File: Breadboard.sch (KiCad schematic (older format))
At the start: 15 parts, among them J201 AudioJack2_SwitchT, J202 AudioJack2_SwitchT, J203 Conn_01x03_Male, J204 Conn_01x03_Male, J205 Power +, J206 Power -, P201 HEADER_2x5_Doepfer

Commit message: Update misc diags
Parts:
- added D?: On LED, AJ:D_0805_AJ, symbol Device:LED
- added J? (x2): Conn_01x03_Male, Connector_PinHeader_2.54mm:PinHeader_1x03_P2.54mm_Vertical, symbol Connector:Conn_01x03_Male
- added J?: AudioJack2_SwitchT, Connector_Audio:Jack_3.5mm_Switronic_ST-005-G_horizontal, symbol Connector:AudioJack2_SwitchT
- added R?: 22k, AJ:R_0805_AJ, symbol Device:R
- added R? (x2): OPEN, AJ:R_0805_AJ, symbol Device:R
- added RV?: 100k, AJ:Potentiometer_China_RK09_Single_Vertical_AJ, symbol Device:R_POT
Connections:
- net GND: now also J?.1 (Pin_1), J?.S
- net at D201.2 (A), R201.2: now also D?.1 (K)
- net at P201.10 (+12), P201.9 (+12), R202.2: now also R?.1
- new net: J?.2 (Pin_2), J?.T
- new net: J?.3 (Pin_3), J?.TN
- new net: D?.2 (A), R?.2
- new net: J?.1 (Pin_1), R?.2, RV?.1
- new net: J?.2 (Pin_2), R?.1, R?.2, RV?.2
- new net: J?.3 (Pin_3), R?.1, RV?.3
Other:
- moved on the sheet: J205, J206
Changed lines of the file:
@@
 L Connector:Conn_01x04_Male J205
 U 1 1 60800BD9
-P 4900 4300
-F 0 "J205" H 4872 4274 50  0000 R CNN
-F 1 "Power +" H 4872 4183 50  0000 R CNN
-F 2 "Connector_PinHeader_2.54mm:PinHeader_2x02_P2.54mm_Vertical" H 4900 4300 50  0001 C CNN
-F 3 "~" H 4900 4300 50  0001 C CNN
-	1    4900 4300
+P 5900 2100
+F 0 "J205" H 5872 2074 50  0000 R CNN
+F 1 "Power +" H 5872 1983 50  0000 R CNN
+F 2 "Connector_PinHeader_2.54mm:PinHeader_2x02_P2.54mm_Vertical" H 5900 2100 50  0001 C CNN
+F 3 "~" H 5900 2100 50  0001 C CNN
+	1    5900 2100
 	-1   0    0    -1
 $EndComp
@@
 L Connector:Conn_01x04_Male J206
 U 1 1 608011E9
-P 4900 4775
-F 0 "J206" H 4872 4749 50  0000 R CNN
-F 1 "Power -" H 4872 4658 50  0000 R CNN
-F 2 "Connector_PinHeader_2.54mm:PinHeader_2x02_P2.54mm_Vertical" H 4900 4775 50  0001 C CNN
-F 3 "~" H 4900 4775 50  0001 C CNN
-	1    4900 4775
-	-1   0    0    -1
-$EndComp
-Wire Wire Line
-	4700 4200 4525 4200
-Wire Wire Line
-	4525 4200 4525 4400
-Wire Wire Line
-	4525 4400 4700 4400
-Wire Wire Line
-	4700 4300 4600 4300
-Wire Wire Line
-	4600 4300 4600 4500
-Wire Wire Line
-	4600 4500 4700 4500
-Wire Wire Line
-	4700 4675 4525 4675
-Wire Wire Line
-	4525 4675 4525 4875
-Wire Wire Line
-	4525 4875 4700 4875
-Wire Wire Line
-	4700 4775 4600 4775
-Wire Wire Line
-	4600 4775 4600 4975
-Wire Wire Line
-	4600 4975 4700 4975
-Text GLabel 4600 4975 0    50   Input ~ 0
+P 5900 2575
+F 0 "J206" H 5872 2549 50  0000 R CNN
+F 1 "Power -" H 5872 2458 50  0000 R CNN
+F 2 "Connector_PinHeader_2.54mm:PinHeader_2x02_P2.54mm_Vertical" H 5900 2575 50  0001 C CNN
+F 3 "~" H 5900 2575 50  0001 C CNN
+	1    5900 2575
+	-1   0    0    -1
+$EndComp
+Wire Wire Line
+	5700 2000 5525 2000
+Wire Wire Line
+	5525 2000 5525 2200
+Wire Wire Line
+	5525 2200 5700 2200
+Wire Wire Line
+	5700 2100 5600 2100
+Wire Wire Line
+	5600 2100 5600 2300
+Wire Wire Line
+	5600 2300 5700 2300
+Wire Wire Line
+	5700 2475 5525 2475
+Wire Wire Line
+	5525 2475 5525 2675
+Wire Wire Line
+	5525 2675 5700 2675
+Wire Wire Line
+	5700 2575 5600 2575
+Wire Wire Line
+	5600 2575 5600 2775
+Wire Wire Line
+	5600 2775 5700 2775
+Text GLabel 5600 2775 0    50   Input ~ 0
 -12Vc
-Text GLabel 4525 4200 0    50   Input ~ 0
+Text GLabel 5525 2000 0    50   Input ~ 0
 +12Vc
 $Comp
 L power:GND #PWR?
 U 1 1 60806A30
-P 4600 4500
+P 5600 2300
 AR Path="/60806A30" Ref="#PWR?"  Part="1"
 AR Path="/607E07E1/60806A30" Ref="#PWR0204"  Part="1"
-F 0 "#PWR0204" H 4600 4250 50  0001 C CNN
-F 1 "GND" H 4605 4327 50  0000 C CNN
-F 2 "" H 4600 4500 50  0001 C CNN
-F 3 "" H 4600 4500 50  0001 C CNN
-	1    4600 4500
+F 0 "#PWR0204" H 5600 2050 50  0001 C CNN
+F 1 "GND" H 5605 2127 50  0000 C CNN
+F 2 "" H 5600 2300 50  0001 C CNN
+F 3 "" H 5600 2300 50  0001 C CNN
+	1    5600 2300
 	1    0    0    -1
 $EndComp
-Connection ~ 4600 4500
-Wire Wire Line
-	4525 4675 4525 4500
-Connection ~ 4525 4675
-Wire Wire Line
-	4525 4500 4600 4500
+Connection ~ 5600 2300
+Wire Wire Line
+	5525 2475 5525 2300
+Connection ~ 5525 2475
+Wire Wire Line
+	5525 2300 5600 2300
 Wire Wire Line
 	3600 2350 4275 2350
@@
 Wire Wire Line
 	3600 2750 4275 2750
+$Comp
+L Connector:Conn_01x03_Male J?
+U 1 1 6086D012
+P 3175 3725
+F 0 "J?" H 3147 3749 50  0000 R CNN
+F 1 "Conn_01x03_Male" H 3147 3658 50  0000 R CNN
+F 2 "Connector_PinHeader_2.54mm:PinHeader_1x03_P2.54mm_Vertical" H 3175 3725 50  0001 C CNN
+F 3 "~" H 3175 3725 50  0001 C CNN
+	1    3175 3725
+	-1   0    0    -1
+$EndComp
+$Comp
+L Connector:AudioJack2_SwitchT J?
+U 1 1 6086D1D0
+P 2425 3725
+F 0 "J?" H 2457 4050 50  0000 C CNN
+F 1 "AudioJack2_SwitchT" H 2457 3959 50  0000 C CNN
+F 2 "Connector_Audio:Jack_3.5mm_Switronic_ST-005-G_horizontal" H 2425 3725 50  0001 C CNN
+F 3 "~" H 2425 3725 50  0001 C CNN
+	1    2425 3725
+	1    0    0    -1
+$EndComp
+Wire Wire Line
+	2625 3625 2825 3625
+Wire Wire Line
+	2625 3725 2975 3725
+Wire Wire Line
+	2625 3825 2975 3825
+Wire Wire Line
+	2825 4225 2825 3625
+Connection ~ 2825 3625
+Wire Wire Line
+	2825 3625 2975 3625
+Wire Wire Line
+	2000 2300 2000 2350
+Wire Wire Line
+	2025 1950 2000 1950
+Wire Wire Line
+	2000 1950 2000 2000
+$Comp
+L Device:R R?
+U 1 1 6086F9BC
+P 2175 1950
+AR Path="/6086F9BC" Ref="R?"  Part="1"
+AR Path="/5C8C5FC0/6086F9BC" Ref="R?"  Part="1"
+AR Path="/5D60ED9A/6086F9BC" Ref="R?"  Part="1"
+AR Path="/60565919/6086F9BC" Ref="R?"  Part="1"
+AR Path="/607E07E1/6086F9BC" Ref="R?"  Part="1"
+F 0 "R?" V 2175 1950 50  0000 C CNN
+F 1 "22k" V 2275 1950 50  0000 C CNN
+F 2 "AJ:R_0805_AJ" V 2105 1950 50  0001 C CNN
+F 3 "~" H 2175 1950 50  0001 C CNN
+	1    2175 1950
+	0    1    1    0
+$EndComp
+$Comp
+L Device:LED D?
+U 1 1 6086F9C6
+P 2000 2150
+AR Path="/5C8BFBBC/6086F9C6" Ref="D?"  Part="1"
+AR Path="/5C8C5FC0/6086F9C6" Ref="D?"  Part="1"
+AR Path="/5D60ED9A/6086F9C6" Ref="D?"  Part="1"
+AR Path="/60565919/6086F9C6" Ref="D?"  Part="1"
+AR Path="/6086F9C6" Ref="D?"  Part="1"
+AR Path="/607E07E1/6086F9C6" Ref="D?"  Part="1"
+F 0 "D?" V 2075 2375 50  0000 R CNN
+F 1 "On LED" V 2000 2425 50  0000 R CNN
+F 2 "AJ:D_0805_AJ" H 2000 2150 50  0001 C CNN
+F 3 "~" H 2000 2150 50  0001 C CNN
+	1    2000 2150
+	0    -1   -1   0
+$EndComp
+Connection ~ 2000 2350
+Wire Wire Line
+	2325 1950 2400 1950
+Connection ~ 2400 1950
+$Comp
+L Device:R_POT RV?
+U 1 1 6088289A
+P 2375 5950
+AR Path="/6165D4D0/6088289A" Ref="RV?"  Part="1"
+AR Path="/607E07E1/6088289A" Ref="RV?"  Part="1"
+F 0 "RV?" H 2306 5996 50  0000 R CNN
+F 1 "100k" H 2306 5905 50  0000 R CNN
+F 2 "AJ:Potentiometer_China_RK09_Single_Vertical_AJ" H 2375 5950 50  0001 C CNN
+F 3 "~" H 2375 5950 50  0001 C CNN
+	1    2375 5950
+	1    0    0    -1
+$EndComp
+Wire Wire Line
+	2375 5575 2375 5800
+$Comp
+L Device:R R?
+U 1 1 608828A5
+P 2700 5750
+AR Path="/608828A5" Ref="R?"  Part="1"
+AR Path="/5C8C5FC0/608828A5" Ref="R?"  Part="1"
+AR Path="/5D60ED9A/608828A5" Ref="R?"  Part="1"
+AR Path="/60565919/608828A5" Ref="R?"  Part="1"
+AR Path="/6165D4D0/608828A5" Ref="R?"  Part="1"
+AR Path="/607E07E1/608828A5" Ref="R?"  Part="1"
+F 0 "R?" V 2700 5700 50  0000 C CNN
+F 1 "OPEN" V 2584 5750 50  0000 C CNN
+F 2 "AJ:R_0805_AJ" V 2630 5750 50  0001 C CNN
+F 3 "~" H 2700 5750 50  0001 C CNN
+	1    2700 5750
+	-1   0    0    1
+$EndComp
+Wire Wire Line
+	2525 5950 2700 5950
+Wire Wire Line
+	2700 5950 2700 5900
+Wire Wire Line
+	2700 5575 2375 5575
+Wire Wire Line
+	2700 5600 2700 5575
+$Comp
+L Device:R R?
+U 1 1 60887755
+P 2700 6175
+AR Path="/60887755" Ref="R?"  Part="1"
+AR Path="/5C8C5FC0/60887755" Ref="R?"  Part="1"
+AR Path="/5D60ED9A/60887755" Ref="R?"  Part="1"
+AR Path="/60565919/60887755" Ref="R?"  Part="1"
+AR Path="/6165D4D0/60887755" Ref="R?"  Part="1"
+AR Path="/607E07E1/60887755" Ref="R?"  Part="1"
+F 0 "R?" V 2700 6125 50  0000 C CNN
+F 1 "OPEN" V 2584 6175 50  0000 C CNN
+F 2 "AJ:R_0805_AJ" V 2630 6175 50  0001 C CNN
+F 3 "~" H 2700 6175 50  0001 C CNN
+	1    2700 6175
+	-1   0    0    1
+$EndComp
+Wire Wire Line
+	2700 5950 2700 6025
+Wire Wire Line
+	2700 6375 2375 6375
+Wire Wire Line
+	2375 6100 2375 6375
+Wire Wire Line
+	2700 6325 2700 6375
+Connection ~ 2700 5950
+$Comp
+L Connector:Conn_01x03_Male J?
+U 1 1 60889921
+P 3300 5950
+F 0 "J?" H 3272 5974 50  0000 R CNN
+F 1 "Conn_01x03_Male" H 3272 5883 50  0000 R CNN
+F 2 "Connector_PinHeader_2.54mm:PinHeader_1x03_P2.54mm_Vertical" H 3300 5950 50  0001 C CNN
+F 3 "~" H 3300 5950 50  0001 C CNN
+	1    3300 5950
+	-1   0    0    -1
+$EndComp
+Wire Wire Line
+	3100 6050 3100 6375
+Wire Wire Line
+	3100 6375 2700 6375
+Connection ~ 2700 6375
+Wire Wire Line
+	3100 5850 3100 5575
+Wire Wire Line
+	3100 5575 2700 5575
+Connection ~ 2700 5575
+Wire Wire Line
+	3100 5950 2700 5950
 $EndSCHEMATC

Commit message: Annotate
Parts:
- added J210: Conn_01x02_Male, Connector_PinHeader_2.54mm:PinHeader_1x02_P2.54mm_Vertical, symbol Connector:Conn_01x02_Male
- added SW201: SW_SPDT, Button_Switch_THT:SW_PUSH_6mm_H8mm, symbol Switch:SW_SPST
- gave numbers to parts that had none: 8
- renumbered D201 to D202, D202 to D203, D203 to D204, J201 to J202, J202 to J203, J205 to J204, J206 to J205, J203 to J207, J204 to J208, R201 to R202, R202 to R203, R203 to R204
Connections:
- new net: J210.1 (Pin_1), SW201.1 (A)
- new net: J210.2 (Pin_2), SW201.2 (B)
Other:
- moved on the sheet: J201, J202, J203, J206, J207, J208, J209, R205, R206, RV201

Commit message: Powerfootprintupdated
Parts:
- C201, C202: footprint Capacitor_SMD:C_1206_3216Metric_Pad1.42x1.75mm_HandSolder -> AJ:C_0805_AJ
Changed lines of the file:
@@
 F 0 "C202" H 3715 2596 50  0000 L CNN
 F 1 "1u" H 3715 2505 50  0000 L CNN
-F 2 "Capacitor_SMD:C_1206_3216Metric_Pad1.42x1.75mm_HandSolder" H 3638 2400 50  0001 C CNN
+F 2 "AJ:C_0805_AJ" H 3638 2400 50  0001 C CNN
 F 3 "~" H 3600 2550 50  0001 C CNN
 	1    3600 2550
@@
 F 0 "C201" H 3715 2196 50  0000 L CNN
 F 1 "1u" H 3715 2105 50  0000 L CNN
-F 2 "Capacitor_SMD:C_1206_3216Metric_Pad1.42x1.75mm_HandSolder" H 3638 2000 50  0001 C CNN
+F 2 "AJ:C_0805_AJ" H 3638 2000 50  0001 C CNN
 F 3 "~" H 3600 2150 50  0001 C CNN
 	1    3600 2150

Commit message: Breadboard routed
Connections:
- net GND: now also D201.1 (K), D202.2 (A); no longer R202.1
- net at P201.1 (-12), P201.2 (-12), R204.2: now also R202.1; no longer D202.1 (K)
- new net: D202.1 (K), R202.2
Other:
- moved on the sheet: R202
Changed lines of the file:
@@
 	2000 2700 2000 2750
 Wire Wire Line
-	2025 2350 2000 2350
-Wire Wire Line
 	2000 2350 2000 2400
-Wire Wire Line
-	2400 2350 2325 2350
 $Comp
 L Device:R R?
 U 1 1 607F4C26
-P 2175 2350
+P 2175 2750
 AR Path="/607F4C26" Ref="R?"  Part="1"
 AR Path="/5C8C5FC0/607F4C26" Ref="R?"  Part="1"
@@
 AR Path="/60565919/607F4C26" Ref="R?"  Part="1"
 AR Path="/607E07E1/607F4C26" Ref="R202"  Part="1"
-F 0 "R202" V 2175 2350 50  0000 C CNN
-F 1 "22k" V 2275 2350 50  0000 C CNN
-F 2 "AJ:R_0805_AJ" V 2105 2350 50  0001 C CNN
-F 3 "~" H 2175 2350 50  0001 C CNN
-	1    2175 2350
+F 0 "R202" V 2175 2750 50  0000 C CNN
+F 1 "22k" V 2275 2750 50  0000 C CNN
+F 2 "AJ:R_0805_AJ" V 2105 2750 50  0001 C CNN
+F 3 "~" H 2175 2750 50  0001 C CNN
+	1    2175 2750
 	0    1    1    0
 $EndComp
@@
 	2500 2450 2500 2350
 Wire Wire Line
-	2000 2750 2400 2750
+	2000 2750 2025 2750
 Wire Wire Line
 	2400 2750 2800 2750
@@
 Wire Wire Line
 	5075 6350 5075 6250
+Wire Wire Line
+	2325 2750 2400 2750
+Wire Wire Line
+	2000 2350 2400 2350
 $EndSCHEMATC

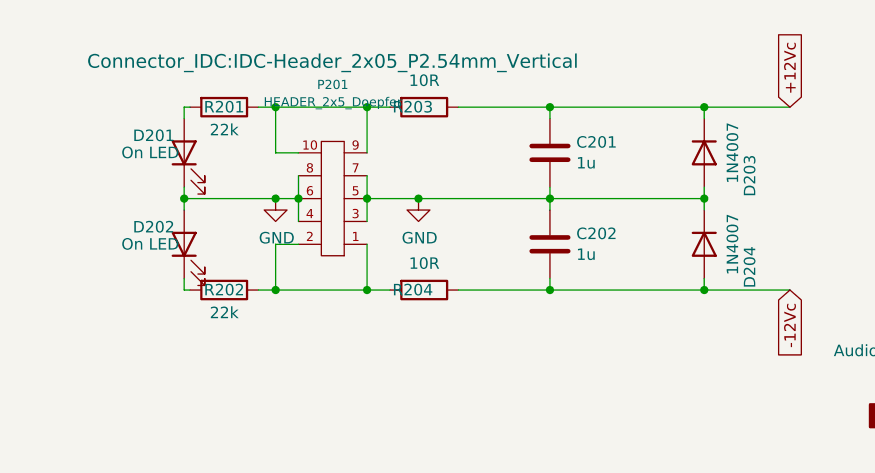
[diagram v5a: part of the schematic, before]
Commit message: decoupling for Op Amp
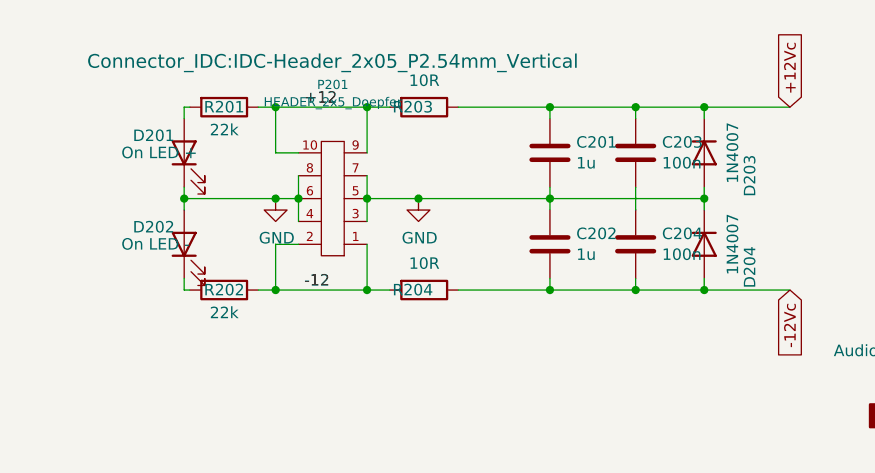
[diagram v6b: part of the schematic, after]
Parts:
- added C203, C204: 100n, AJ:C_0805_AJ, symbol Device:C
- D201: value On LED -> On LED +
- D202: value On LED -> On LED -
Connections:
- net +12Vc: now also C203.1
- net -12Vc: now also C204.2
- net -12: now reaches P201.1 (-12), P201.2 (-12), R202.1, R204.2
- net +12: now reaches P201.10 (+12), P201.9 (+12), R201.1, R203.2
- new net: C203.2, C204.1
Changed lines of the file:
@@
 AR Path="/607E07E1/607F4C2C" Ref="D202"  Part="1"
 F 0 "D202" V 2075 2775 50  0000 R CNN
-F 1 "On LED" V 2000 2825 50  0000 R CNN
+F 1 "On LED -" V 2000 2825 50  0000 R CNN
 F 2 "AJ:D_0805_AJ" H 2000 2550 50  0001 C CNN
 F 3 "~" H 2000 2550 50  0001 C CNN
@@
 	3600 2350 4275 2350
 Wire Wire Line
-	3600 1950 4275 1950
-Wire Wire Line
-	3600 2750 4275 2750
+	3600 1950 3975 1950
+Wire Wire Line
+	3600 2750 3975 2750
 $Comp
 L Connector:Conn_01x03_Male J206
@@
 AR Path="/607E07E1/6086F9C6" Ref="D201"  Part="1"
 F 0 "D201" V 2075 2375 50  0000 R CNN
-F 1 "On LED" V 2000 2425 50  0000 R CNN
+F 1 "On LED +" V 2000 2425 50  0000 R CNN
 F 2 "AJ:D_0805_AJ" H 2000 2150 50  0001 C CNN
 F 3 "~" H 2000 2150 50  0001 C CNN
@@
 Wire Wire Line
 	2000 2350 2400 2350
+Text Label 2525 1950 0    50   ~ 0
++12
+Text Label 2525 2750 0    50   ~ 0
+-12
+$Comp
+L Device:C C203
+U 1 1 60B154B9
+P 3975 2150
+F 0 "C203" H 4090 2196 50  0000 L CNN
+F 1 "100n" H 4090 2105 50  0000 L CNN
+F 2 "AJ:C_0805_AJ" H 4013 2000 50  0001 C CNN
+F 3 "~" H 3975 2150 50  0001 C CNN
+	1    3975 2150
+	1    0    0    -1
+$EndComp
+$Comp
+L Device:C C204
+U 1 1 60B15B12
+P 3975 2550
+F 0 "C204" H 4090 2596 50  0000 L CNN
+F 1 "100n" H 4090 2505 50  0000 L CNN
+F 2 "AJ:C_0805_AJ" H 4013 2400 50  0001 C CNN
+F 3 "~" H 3975 2550 50  0001 C CNN
+	1    3975 2550
+	1    0    0    -1
+$EndComp
+Wire Wire Line
+	3975 2750 3975 2700
+Wire Wire Line
+	3975 2000 3975 1950
+Wire Wire Line
+	3975 2400 3975 2300
+Connection ~ 3975 2750
+Wire Wire Line
+	3975 2750 4275 2750
+Connection ~ 3975 1950
+Wire Wire Line
+	3975 1950 4275 1950
 $EndSCHEMATC

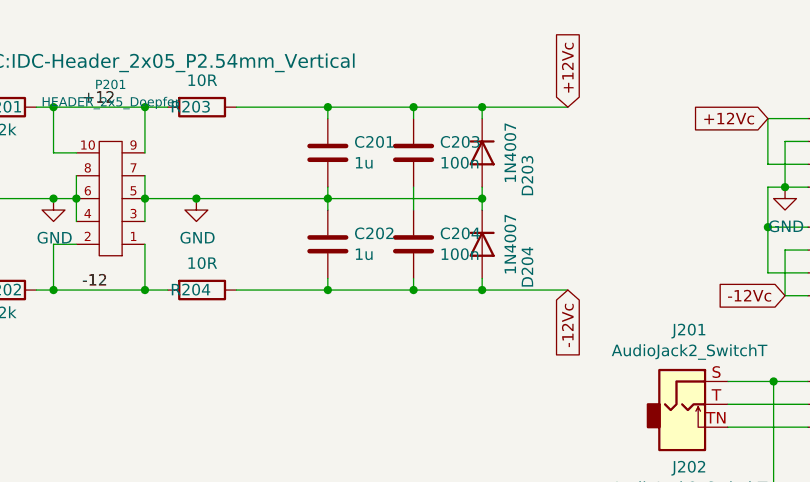
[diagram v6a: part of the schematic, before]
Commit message: BB Logo - GND planes
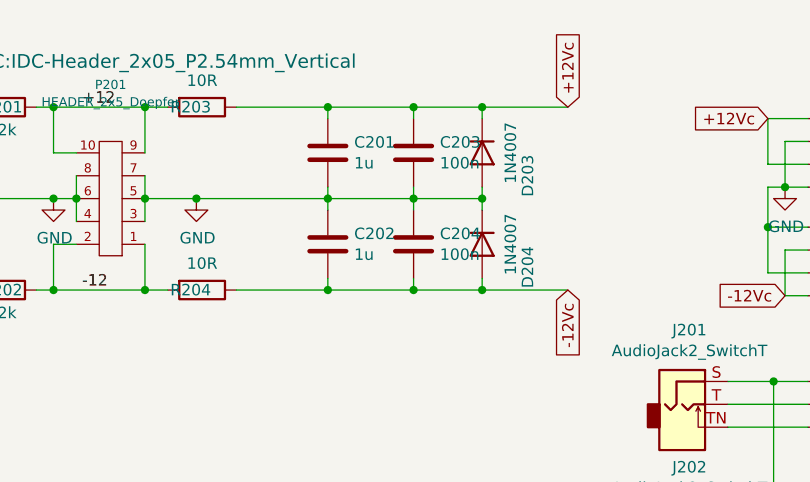
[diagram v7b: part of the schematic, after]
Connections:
- net GND: now also C203.2, C204.1
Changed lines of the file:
@@
 	5525 2300 5600 2300
 Wire Wire Line
-	3600 2350 4275 2350
+	3600 2350 3975 2350
 Wire Wire Line
 	3600 1950 3975 1950
@@
 Wire Wire Line
 	3975 2000 3975 1950
-Wire Wire Line
-	3975 2400 3975 2300
 Connection ~ 3975 2750
 Wire Wire Line
@@
 Wire Wire Line
 	3975 1950 4275 1950
+Wire Wire Line
+	3975 2300 3975 2350
+Connection ~ 3975 2350
+Wire Wire Line
+	3975 2350 4275 2350
+Wire Wire Line
+	3975 2350 3975 2400
 $EndSCHEMATC
